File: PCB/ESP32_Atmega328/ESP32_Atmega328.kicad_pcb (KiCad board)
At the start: 4 copper layers, 55.2 x 52.5 mm, 25 parts, among them J1 ESP_CONN, J2 PWR_CONN, J3 Conn_01x05, SW1 SW_SPDT

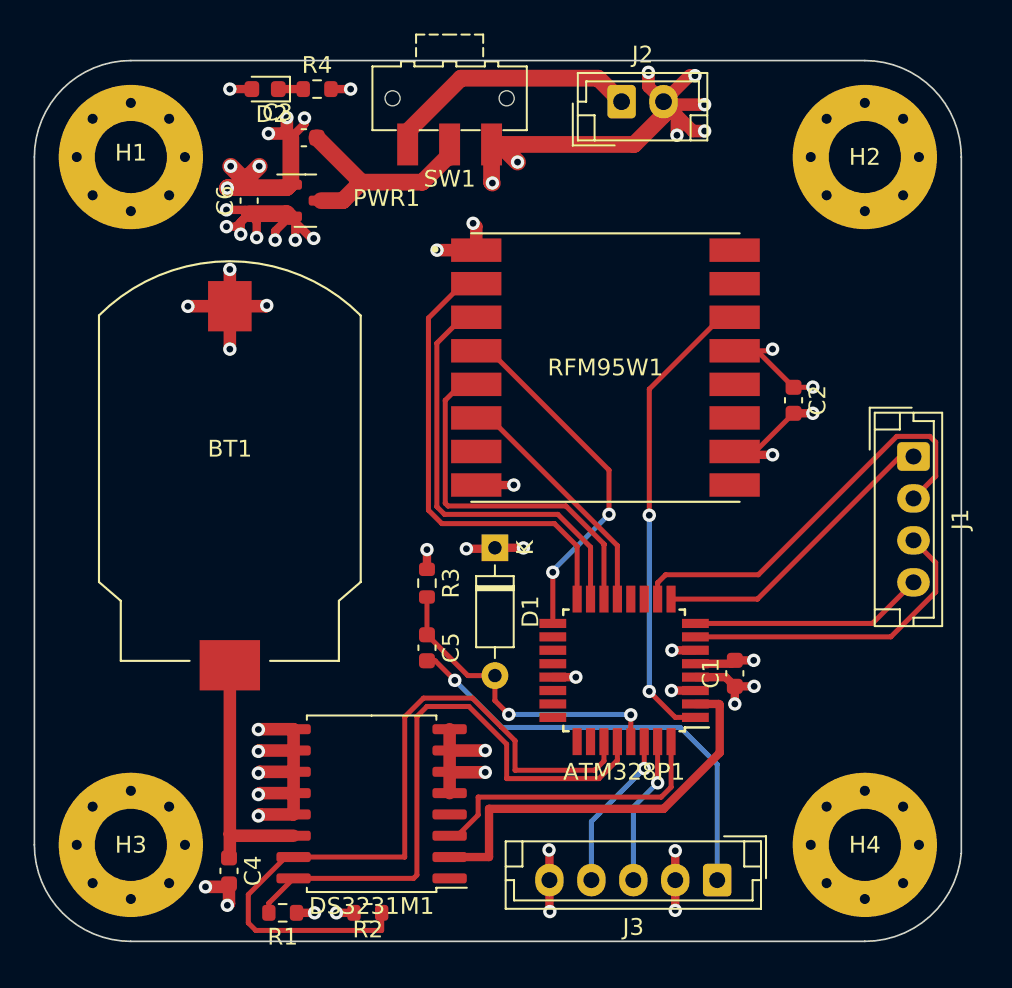
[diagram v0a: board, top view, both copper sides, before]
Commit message: Added parts, rerouted some, added component zips
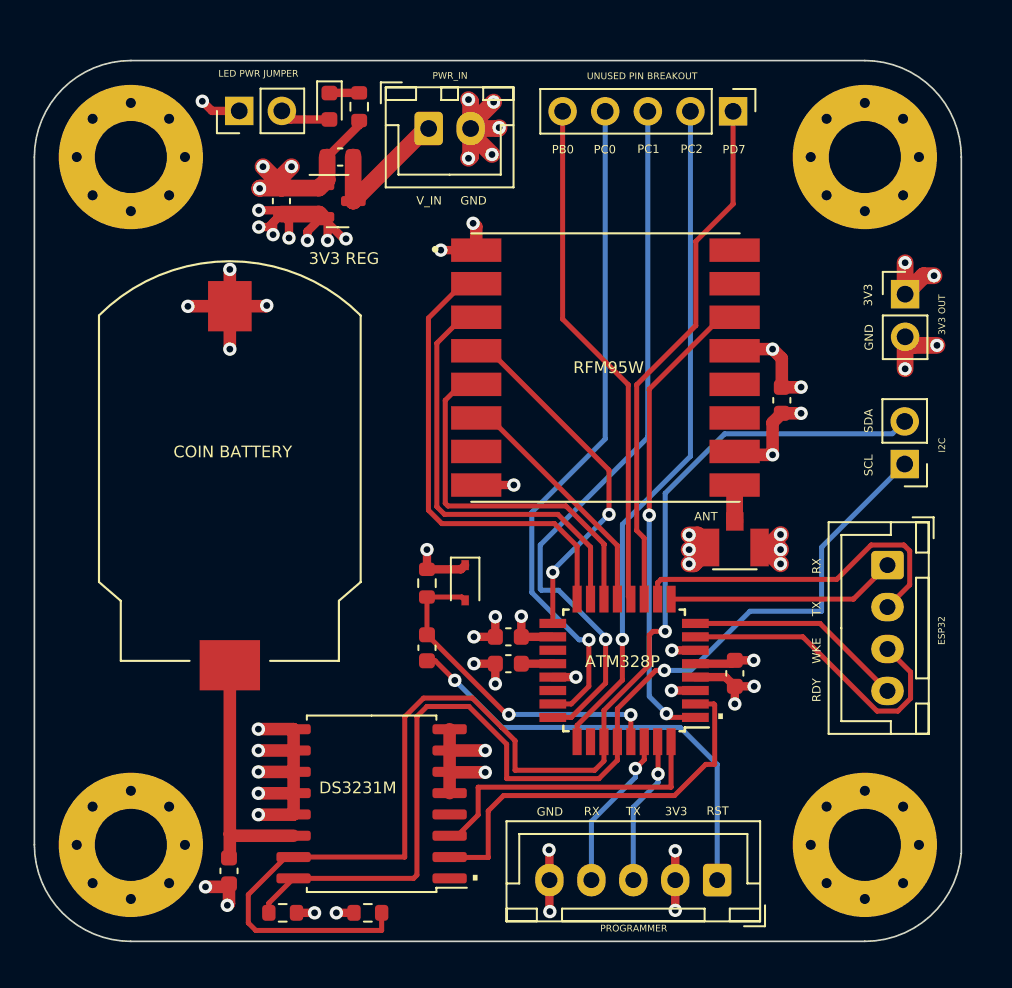
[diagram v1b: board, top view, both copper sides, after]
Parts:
- removed SW1: SW_SPDT, Button_Switch_SMD:SW_SPDT_CK-JS102011SAQN
- added C7: 100n, Capacitor_SMD:C_0603_1608Metric, F.Cu at (126.0, 112.1)
- added C8: 100n, Capacitor_SMD:C_0603_1608Metric, F.Cu at (126.0, 113.7)
- added J4: U.FL-R-SMT(01), footprints:HRS_U.FL-R-SMT(01), F.Cu at (139.5, 106.8)
- added J5: I2C_CONN, Connector_PinHeader_2.54mm:PinHeader_1x02_P2.54mm_Vertical, F.Cu at (149.6, 101.8)
- added J6: BREAKOUT_CONN, Connector_PinHeader_2.54mm:PinHeader_1x05_P2.54mm_Vertical, F.Cu at (139.4, 80.8)
- added J7: PWR_OUT_CONN, Connector_PinHeader_2.54mm:PinHeader_1x02_P2.54mm_Vertical, F.Cu at (149.7, 91.7)
- added JP1: Jumper_2_Open, Connector_PinHeader_2.54mm:PinHeader_1x02_P2.54mm_Vertical, F.Cu at (110.0, 80.8)
- D1: footprint Diode_THT:D_DO-35_SOD27_P7.62mm_Horizontal -> Diode_SMD:D_SOD-323
- J1: footprint Connector_JST:JST_EH_B4B-EH-A_1x04_P2.50mm_Vertical -> Connector_JST:JST_XH_B4B-XH-A_1x04_P2.50mm_Vertical
- J2: value PWR_CONN -> PWR_IN_CONN; footprint Connector_JST:JST_EH_B2B-EH-A_1x02_P2.50mm_Vertical -> Connector_JST:JST_XH_B2B-XH-A_1x02_P2.50mm_Vertical
- J3: value Conn_01x05 -> PROG_CONN; footprint Connector_JST:JST_EH_B5B-EH-A_1x05_P2.50mm_Vertical -> Connector_JST:JST_XH_B5B-XH-A_1x05_P2.50mm_Vertical
- moved J2 11.6 mm to (121.2, 81.8)
- moved J1 6.66 mm to (148.6, 107.8)
- moved D2 3.97 mm to (115.3, 80.5), turned to -90 degrees
- moved D1 2.74 mm to (123.4, 108.9)
- moved R4 2.72 mm to (117.1, 80.5), turned to -90 degrees
- moved C3 2.45 mm to (116.0, 83.5)
- moved C6 1.93 mm to (112.5, 86.1)
- moved PWR1 1.93 mm to (115.8, 86.1)
- moved C2 0.70 mm to (142.3, 98.0)
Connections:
- net CLOCK_SCL renamed I2C_SCL
- net CLOCK_SDA renamed I2C_SDA
- ATM328P1 pad 11: unconnected-(ATM328P1-Pad11) -> PD7
- ATM328P1 pad 12: unconnected-(ATM328P1-Pad12) -> PB0
- ATM328P1 pad 18: unconnected-(ATM328P1-Pad18) -> +3V3
- ATM328P1 pad 20: unconnected-(ATM328P1-Pad20) -> Net-(ATM328P1-Pad20)
- ATM328P1 pad 23: unconnected-(ATM328P1-Pad23) -> PC0
- ATM328P1 pad 24: unconnected-(ATM328P1-Pad24) -> PC1
- ATM328P1 pad 25: unconnected-(ATM328P1-Pad25) -> PC2
- C3 pad 1: Net-(PWR1-Pad3) -> +6V
- D2 pad 2: +3V3 -> Net-(D2-Pad2)
- PWR1 pad 3: Net-(PWR1-Pad3) -> +6V
- RFM95W1 pad 9: unconnected-(RFM95W1-Pad9) -> RFM_ANT
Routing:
- net PC1: track 0.00 -> 43.0 mm, vias 0 -> 1
- net PC0: track 0.00 -> 40.4 mm, vias 0 -> 1
- net PC2: track 0.00 -> 40.4 mm, vias 0 -> 1
- net I2C_SDA: track 46.0 -> 78.8 mm, vias 0 -> 1
- net PD7: track 0.00 -> 31.6 mm
- net PB0: track 0.00 -> 30.8 mm
- net I2C_SCL: track 36.3 -> 63.7 mm, vias 0 -> 1
- net Net-(PWR1-Pad3): track 13.9 -> 0.00 mm
- net GND: track 104.4 -> 97.6 mm, vias 37 -> 43
- net +6V: track 15.4 -> 8.91 mm
- net +3V3: track 39.6 -> 44.9 mm, vias 20 -> 21
- net ATM_TXD_SS: track 25.2 -> 21.0 mm
- net ATM_RXD_SS: track 18.0 -> 13.7 mm
- net Net-(D2-Pad2): track 0.00 -> 3.05 mm
- net RFM_ANT: track 0.00 -> 2.18 mm
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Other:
- board text added: "."
- board text added: "3V3"
- board text added: "3V3 OUT"
- board text added: "3V3 REG"
- board text added: "ANT"
- board text added: "ATM328P"
- board text added: "COIN BATTERY"
- board text added: "CottonCandy Node PCB PCB Design & Layout by Alex Bogdan CottonCandy by Dison Wu Copyright © 2022"
- board text added: "DS3231M"
- board text added: "ESP32"
- board text added: "GND"
- board text added: "I2C"
- board text added: "LED PWR JUMPER"
- board text added: "PB0"
- board text added: "PC0"
- board text added: "PC1"
- board text added: "PC2"
- board text added: "PD7"
- board text added: "PROGRAMMER"
- board text added: "PWR_IN"
- board text added: "RDY"
- board text added: "RFM95W"
- board text added: "RST"
- board text added: "RX"
- board text added: "SCL"
- board text added: "SDA"
- board text added: "TX"
- board text added: "UNUSED PIN BREAKOUT"
- board text added: "V_IN"
- board text added: "WKE"

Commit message: Antenna impedance matching to 50ohms, and added more ground vias around the antenna connector
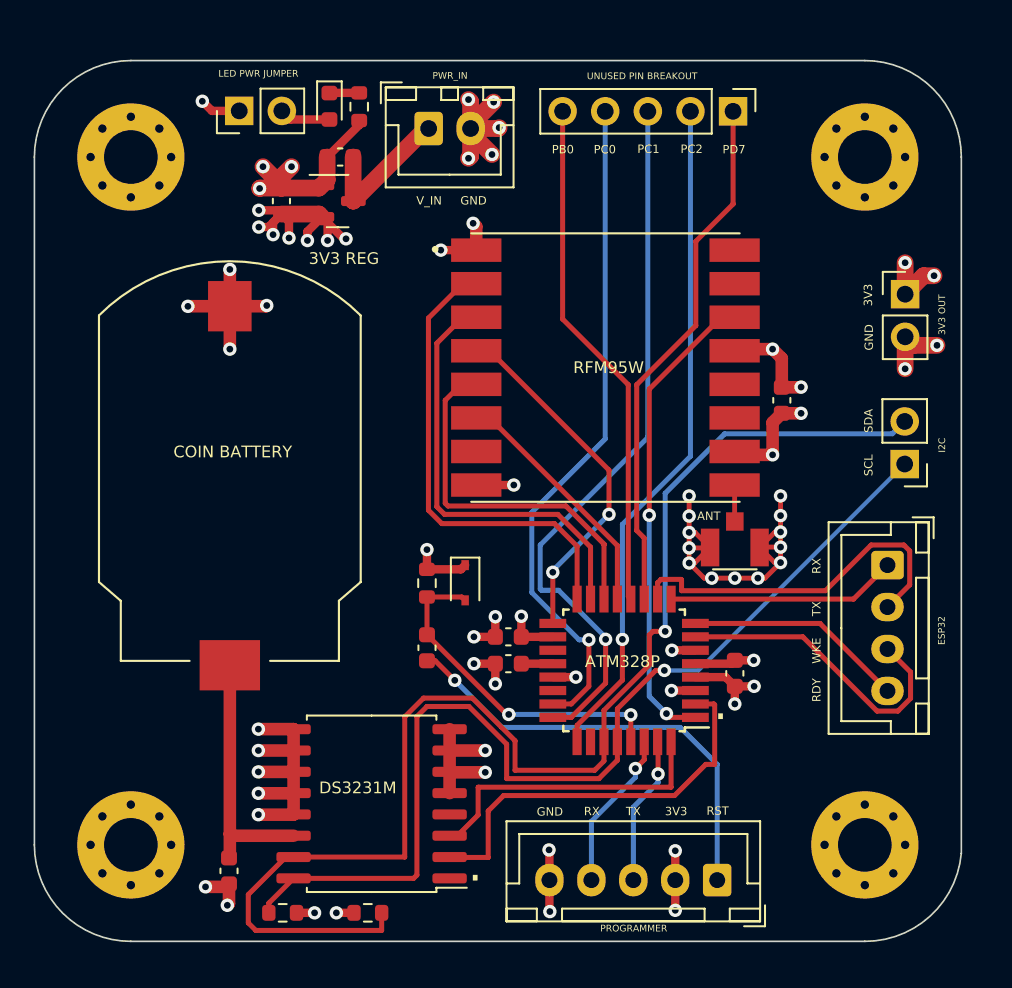
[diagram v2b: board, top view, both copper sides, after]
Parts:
- H1, H2, H3, H4: footprint MountingHole:MountingHole_4.3mm_M4_Pad_Via -> MountingHole:MountingHole_3.2mm_M3_Pad_Via
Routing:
- net GND: track 97.6 -> 111.8 mm, vias 43 -> 50
- net I2C_SCL: track 63.7 -> 61.4 mm
- net ATM_TXD_SS: track 21.0 -> 21.9 mm
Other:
- board text added: "CottonCandy Node PCB PCB Design & Layout by Alex Bogdan CottonCandy by Dison Wu University of Toronto Network Research Lab Copyright © 2022"
- board text removed: "CottonCandy Node PCB PCB Design & Layout by Alex Bogdan CottonCandy by Dison Wu Copyright © 2022"
